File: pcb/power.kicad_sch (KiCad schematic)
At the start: 24 parts, among them J9 Conn_01x02, Q1 MOT S8050/J3Y/0.4, U5 BQ24074RGT, U6 RT9167A-33GB

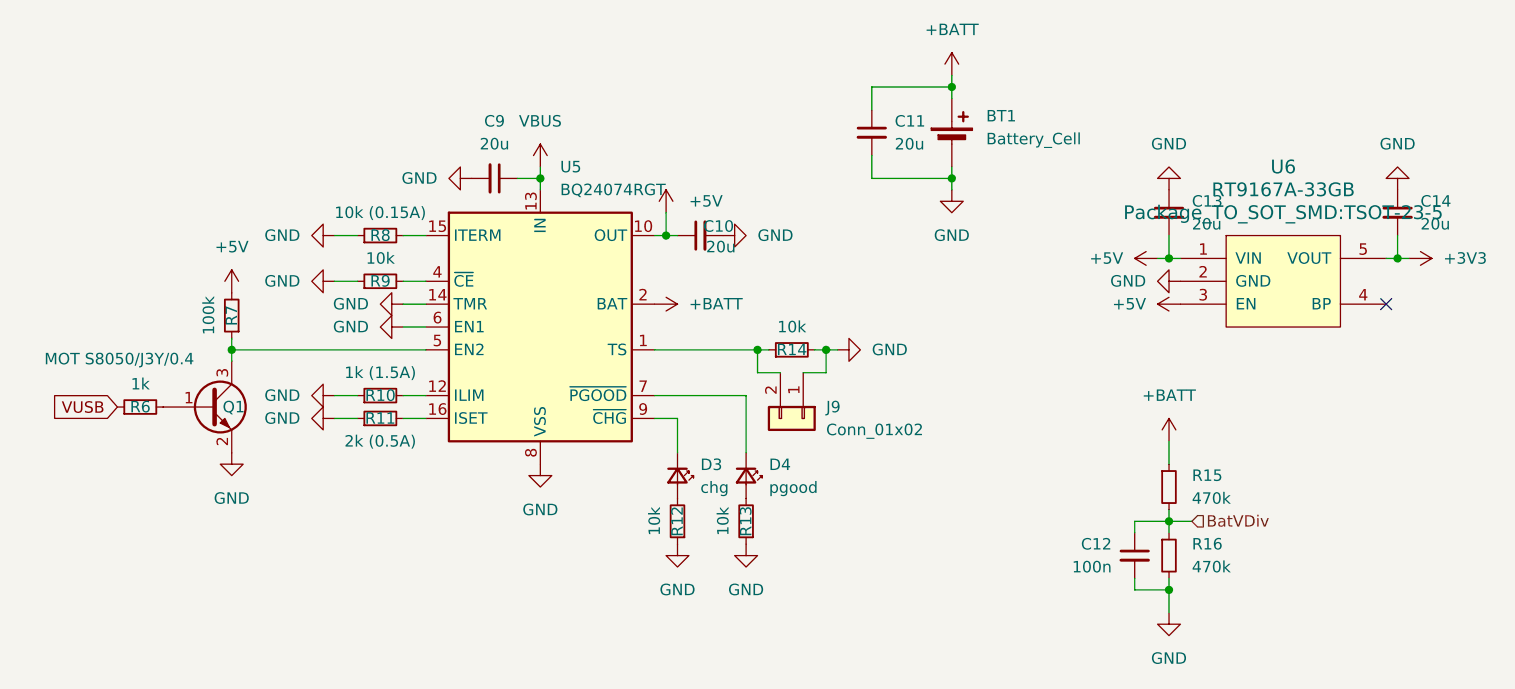
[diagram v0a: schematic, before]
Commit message: Rename pcb, add sensors and fix some issues
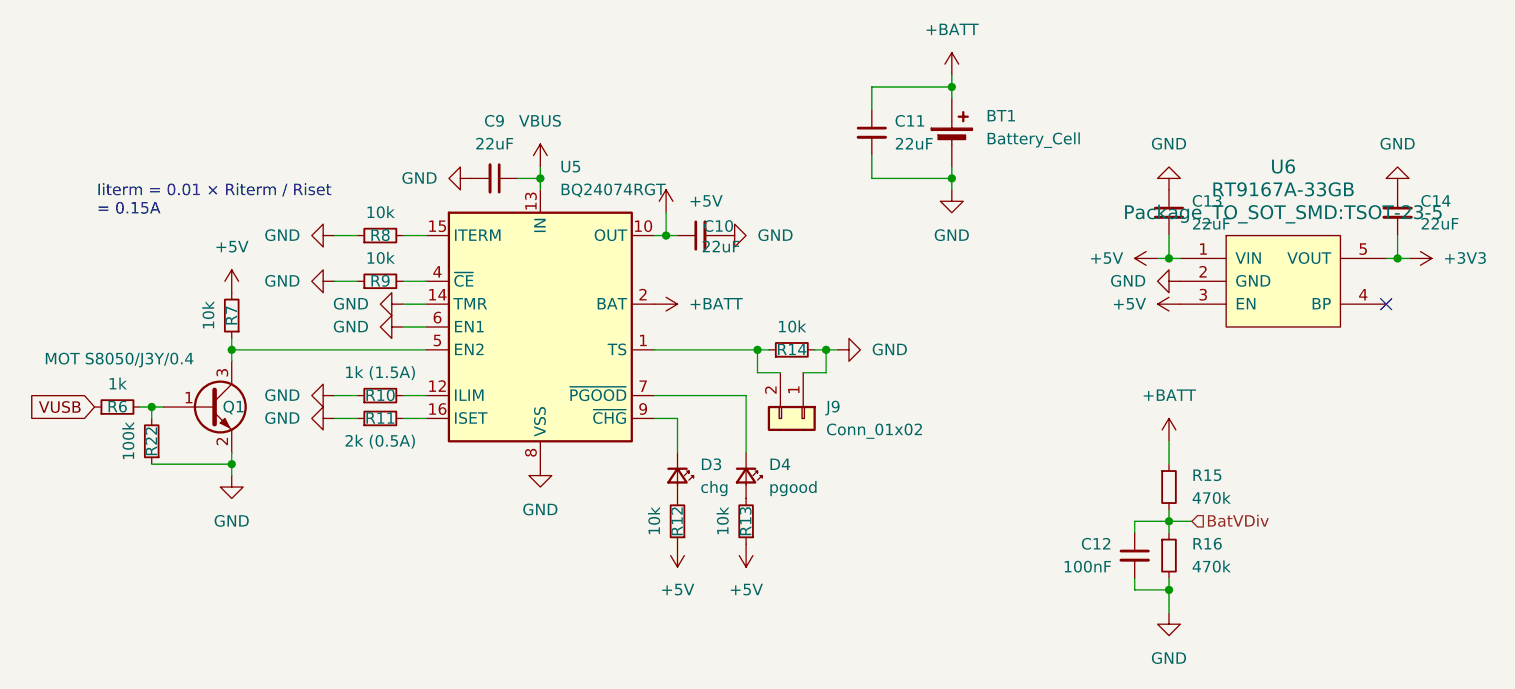
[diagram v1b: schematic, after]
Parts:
- added R22: 100k, Resistor_SMD:R_0603_1608Metric, symbol Device:R_Small
- C10, C11, C13, C14, C9: value 20u -> 22uF
- C12: value 100n -> 100nF
- R7: value 100k -> 10k
- R8: value 10k (0.15A) -> 10k
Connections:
- net +5V: now also R12.1, R13.1
- net GND: now also R22.1; no longer R12.1, R13.1
- net at Q1.1 (B), R6.2: now also R22.2
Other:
- note added: "Iiterm = 0.01 × Riterm / Riset = 0.15A"
- moved on the sheet: R6
